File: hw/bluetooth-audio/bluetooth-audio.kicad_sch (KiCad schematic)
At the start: 0 parts

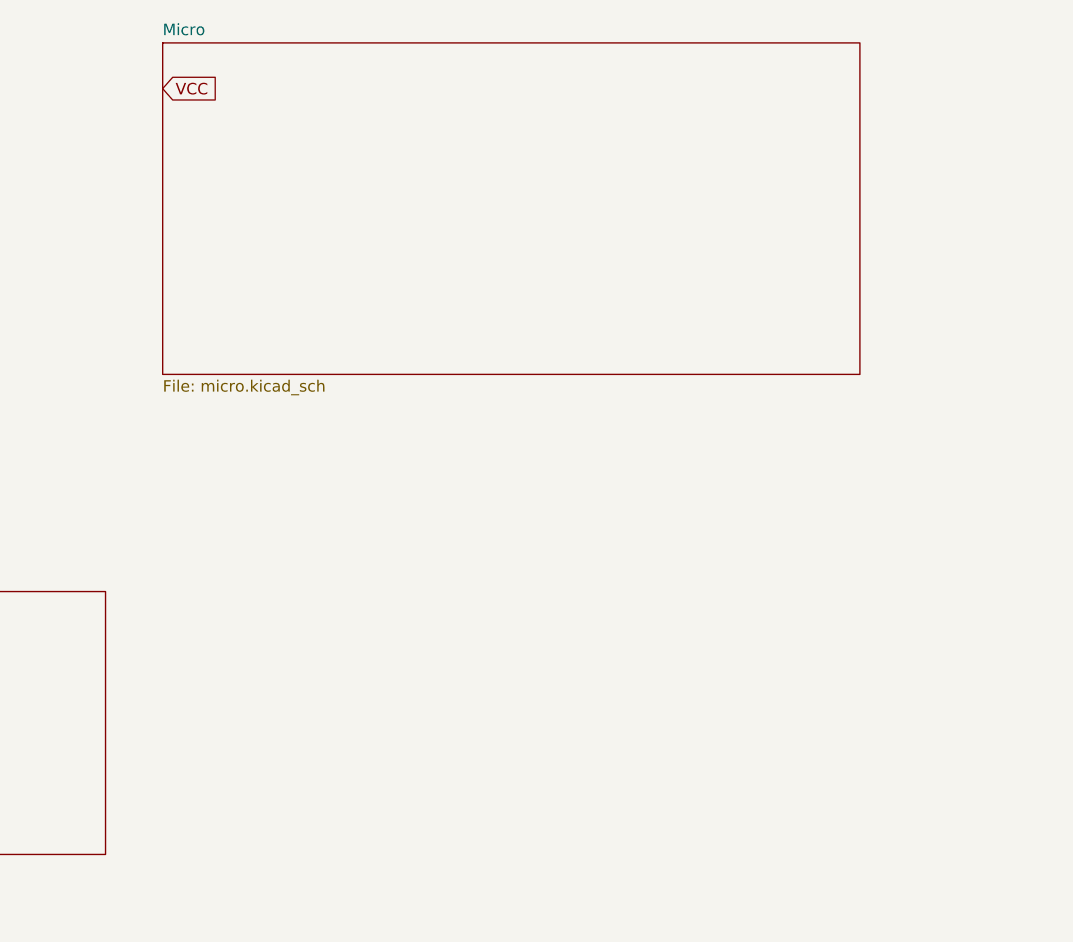
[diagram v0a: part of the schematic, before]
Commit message: Custom symbol and footprints for IS2083. Updated design document. Initial dump of components onto cleared PCB.
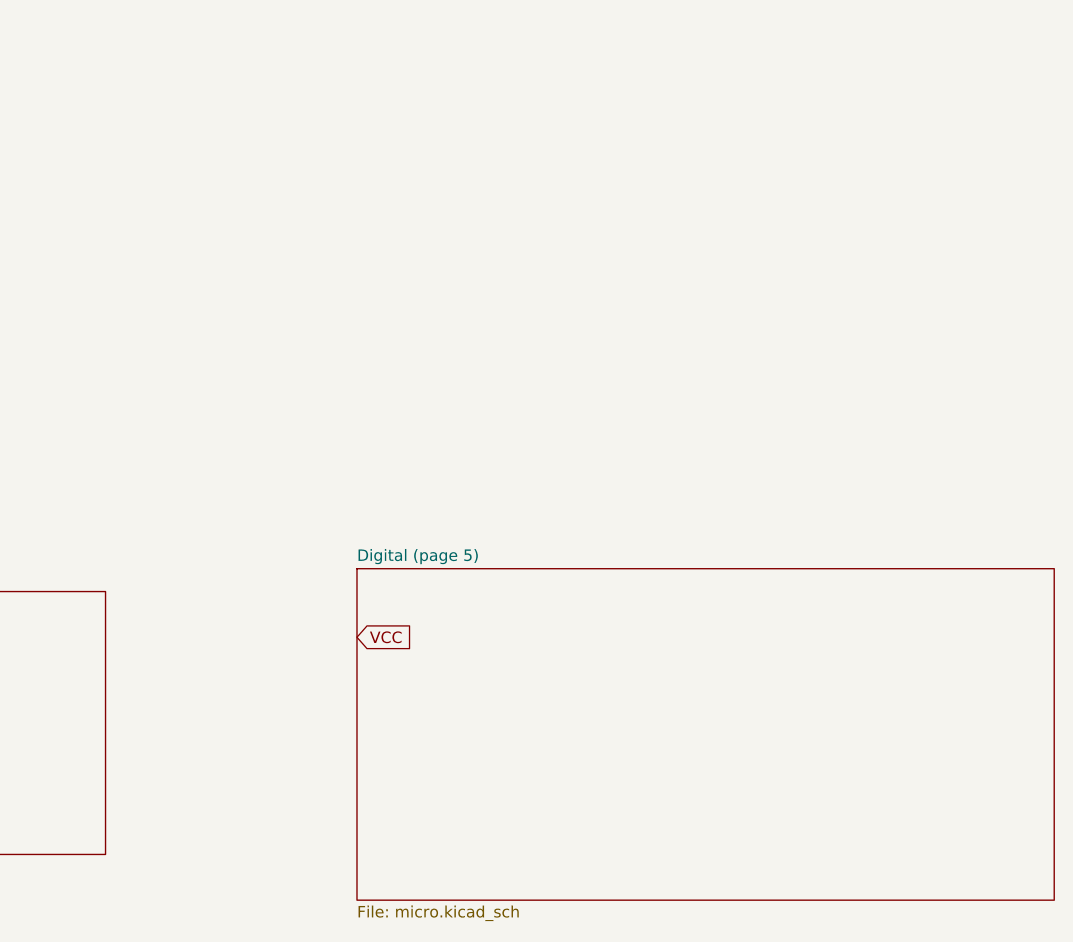
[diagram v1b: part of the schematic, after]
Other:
- removed sheet Micro
- added sheet Digital (page 5) (micro.kicad_sch)
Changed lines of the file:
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@@
+	(global_label "VCC"
+		(shape input)
+		(at 143.51 102.87 0)
+		(fields_autoplaced yes)
+		(effects
+			(font
+				(size 1.27 1.27)
+			)
+			(justify left)
+		)
+		(property "Intersheetrefs" "${INTERSHEET_REFS}"
+			(at 150.1238 102.87 0)
+			(effects
+				(font
+					(size 1.27 1.27)
+				)
+				(justify left)
+				(hide yes)
+			)
+		)
+	)
 	(global_label "VCC"
 		(shape input)
@@
 				)
 				(justify right)
-				(hide yes)
-			)
-		)
-	)
-	(global_label "VCC"
-		(shape input)
-		(at 121.92 41.91 0)
-		(fields_autoplaced yes)
-		(effects
-			(font
-				(size 1.27 1.27)
-			)
-			(justify left)
-		)
-		(property "Intersheetrefs" "${INTERSHEET_REFS}"
-			(at 128.5338 41.91 0)
-			(effects
-				(font
-					(size 1.27 1.27)
-				)
-				(justify left)
 				(hide yes)
 			)
@@
 	)
 	(sheet
-		(at 121.92 36.83)
+		(at 143.51 95.25)
 		(size 77.47 36.83)
 		(exclude_from_sim no)
@@
 			(color 255 255 194 1.0000)
 		)
-		(property "Sheetname" "Micro"
-			(at 121.92 36.1184 0)
+		(property "Sheetname" "Digital (page 5)"
+			(at 143.51 94.5384 0)
 			(effects
 				(font
@@
 		)
 		(property "Sheetfile" "micro.kicad_sch"
-			(at 121.92 74.2446 0)
+			(at 143.51 132.6646 0)
 			(effects
 				(font
@@
 			(project "bluetooth-audio"
 				(path "/eafc8824-f117-40b2-99b0-597946d6c01d"
-					(page "3")
+					(page "5")
 				)
 			)

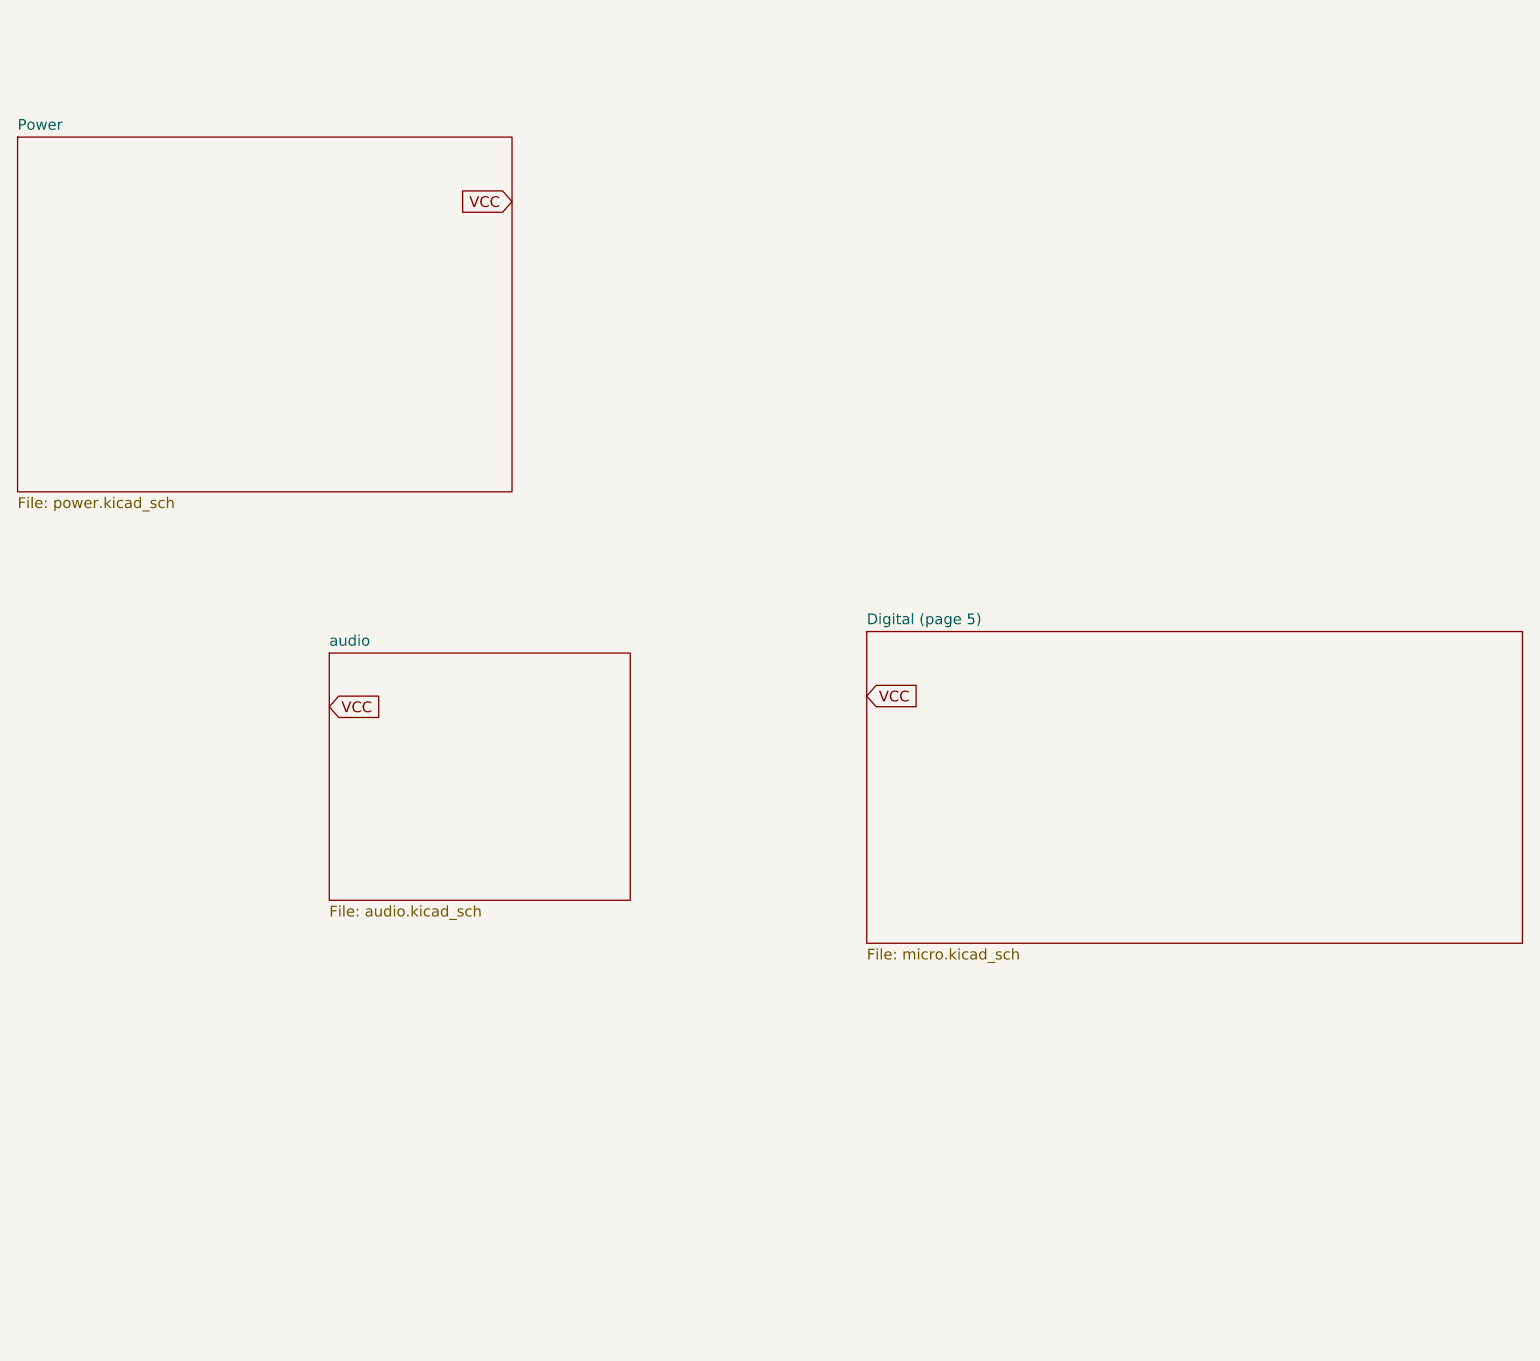
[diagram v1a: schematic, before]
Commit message: All decoupling caps and labels on IS2083
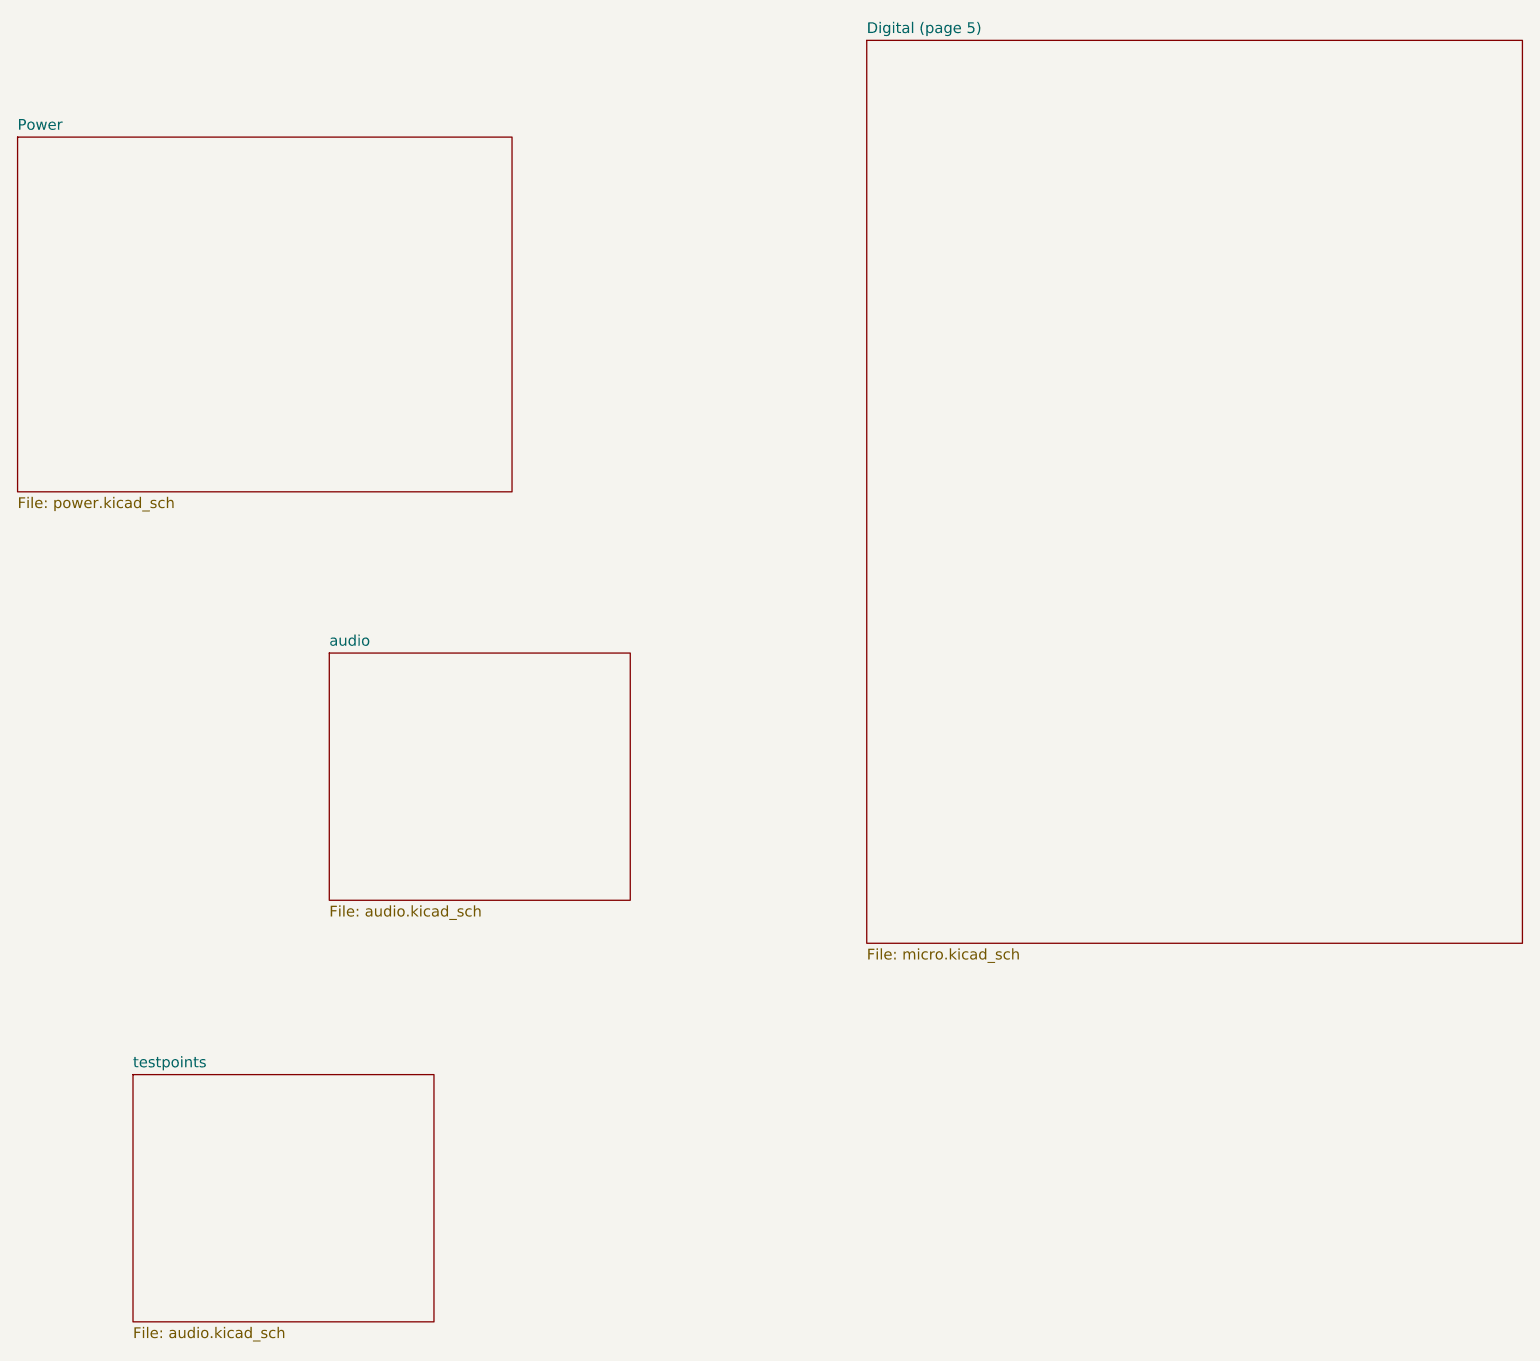
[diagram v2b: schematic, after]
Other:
- added sheet testpoints (audio.kicad_sch)
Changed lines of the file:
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@@
 	(generator_version "9.0")
 	(paper "A4")
-	(global_label "VCC"
-		(shape input)
-		(at 143.51 102.87 0)
-		(fields_autoplaced yes)
-		(effects
-			(font
-				(size 1.27 1.27)
-			)
-			(justify left)
-		)
-		(property "Intersheetrefs" "${INTERSHEET_REFS}"
-			(at 150.1238 102.87 0)
-			(effects
-				(font
-					(size 1.27 1.27)
-				)
-				(justify left)
-				(hide yes)
-			)
-		)
-	)
-	(global_label "VCC"
-		(shape input)
-		(at 101.6 44.45 180)
-		(fields_autoplaced yes)
-		(effects
-			(font
-				(size 1.27 1.27)
-			)
-			(justify right)
-		)
-		(property "Intersheetrefs" "${INTERSHEET_REFS}"
-			(at 94.9862 44.45 0)
-			(effects
-				(font
-					(size 1.27 1.27)
-				)
-				(justify right)
-				(hide yes)
-			)
-		)
-	)
-	(global_label "VCC"
-		(shape input)
-		(at 80.01 104.14 0)
-		(fields_autoplaced yes)
-		(effects
-			(font
-				(size 1.27 1.27)
-			)
-			(justify left)
-		)
-		(property "Intersheetrefs" "${INTERSHEET_REFS}"
-			(at 86.6238 104.14 0)
-			(effects
-				(font
-					(size 1.27 1.27)
-				)
-				(justify left)
-				(hide yes)
-			)
-		)
-	)
 	(sheet
 		(at 80.01 97.79)
@@
 	)
 	(sheet
-		(at 143.51 95.25)
-		(size 77.47 36.83)
+		(at 56.8182 147.5975)
+		(size 35.56 29.21)
+		(exclude_from_sim no)
+		(in_bom yes)
+		(on_board yes)
+		(dnp no)
+		(fields_autoplaced yes)
+		(stroke
+			(width 0.1524)
+			(type solid)
+		)
+		(fill
+			(color 255 255 194 1.0000)
+		)
+		(property "Sheetname" "testpoints"
+			(at 56.8182 146.8859 0)
+			(effects
+				(font
+					(size 1.27 1.27)
+				)
+				(justify left bottom)
+			)
+		)
+		(property "Sheetfile" "audio.kicad_sch"
+			(at 56.8182 177.3921 0)
+			(effects
+				(font
+					(size 1.27 1.27)
+				)
+				(justify left top)
+			)
+		)
+		(instances
+			(project "bluetooth-audio"
+				(path "/eafc8824-f117-40b2-99b0-597946d6c01d"
+					(page "3")
+				)
+			)
+		)
+	)
+	(sheet
+		(at 143.51 25.4)
+		(size 77.47 106.68)
 		(exclude_from_sim no)
 		(in_bom yes)
@@
 		)
 		(property "Sheetname" "Digital (page 5)"
-			(at 143.51 94.5384 0)
+			(at 143.51 24.6884 0)
 			(effects
 				(font

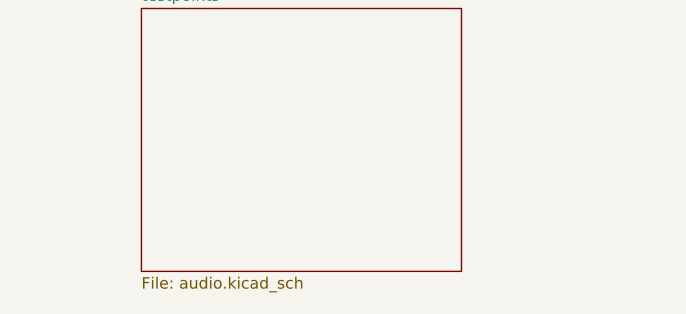
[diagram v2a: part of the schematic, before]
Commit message: Fixing sheet titles
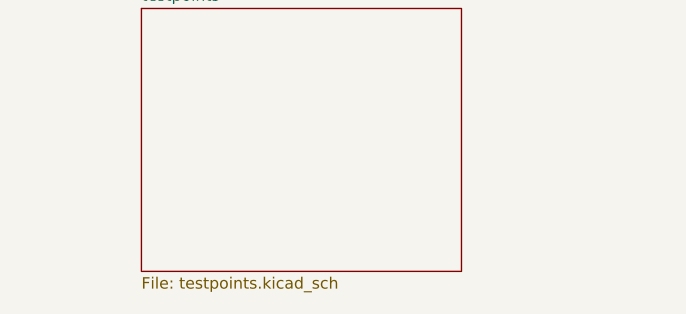
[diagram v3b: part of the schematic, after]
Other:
- sheet testpoints: file audio.kicad_sch -> testpoints.kicad_sch
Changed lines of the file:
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@@
 			)
 		)
-		(property "Sheetfile" "audio.kicad_sch"
+		(property "Sheetfile" "testpoints.kicad_sch"
 			(at 56.8182 177.3921 0)
 			(effects

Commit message: TODO diff
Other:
- sheet Digital (page 5) renamed Digital
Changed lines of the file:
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@@
 			(color 255 255 194 1.0000)
 		)
-		(property "Sheetname" "Digital (page 5)"
+		(property "Sheetname" "Digital"
 			(at 143.51 24.6884 0)
 			(effects
